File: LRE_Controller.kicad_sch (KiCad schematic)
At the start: 14 parts, among them U1 TPS56A37RPAR

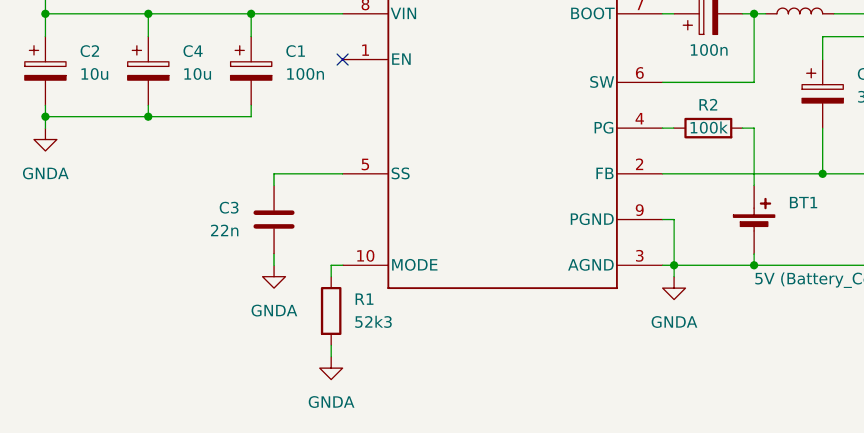
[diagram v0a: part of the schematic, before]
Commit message: Added Microcontroller and pressure transducer.
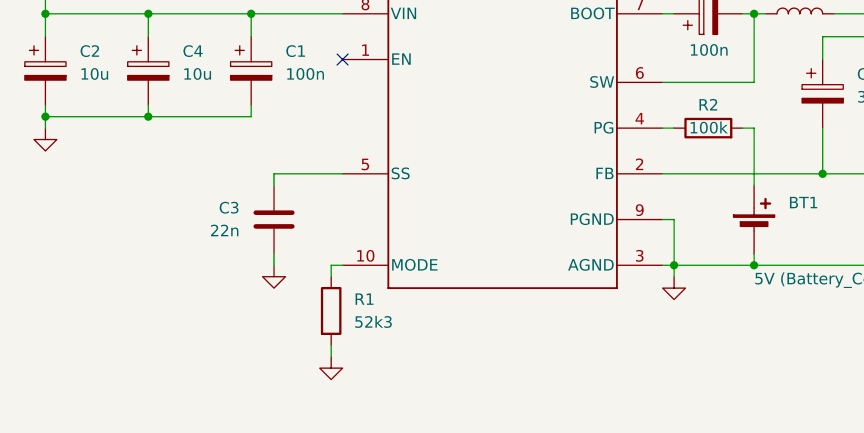
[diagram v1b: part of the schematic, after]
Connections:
- net GNDA renamed GND

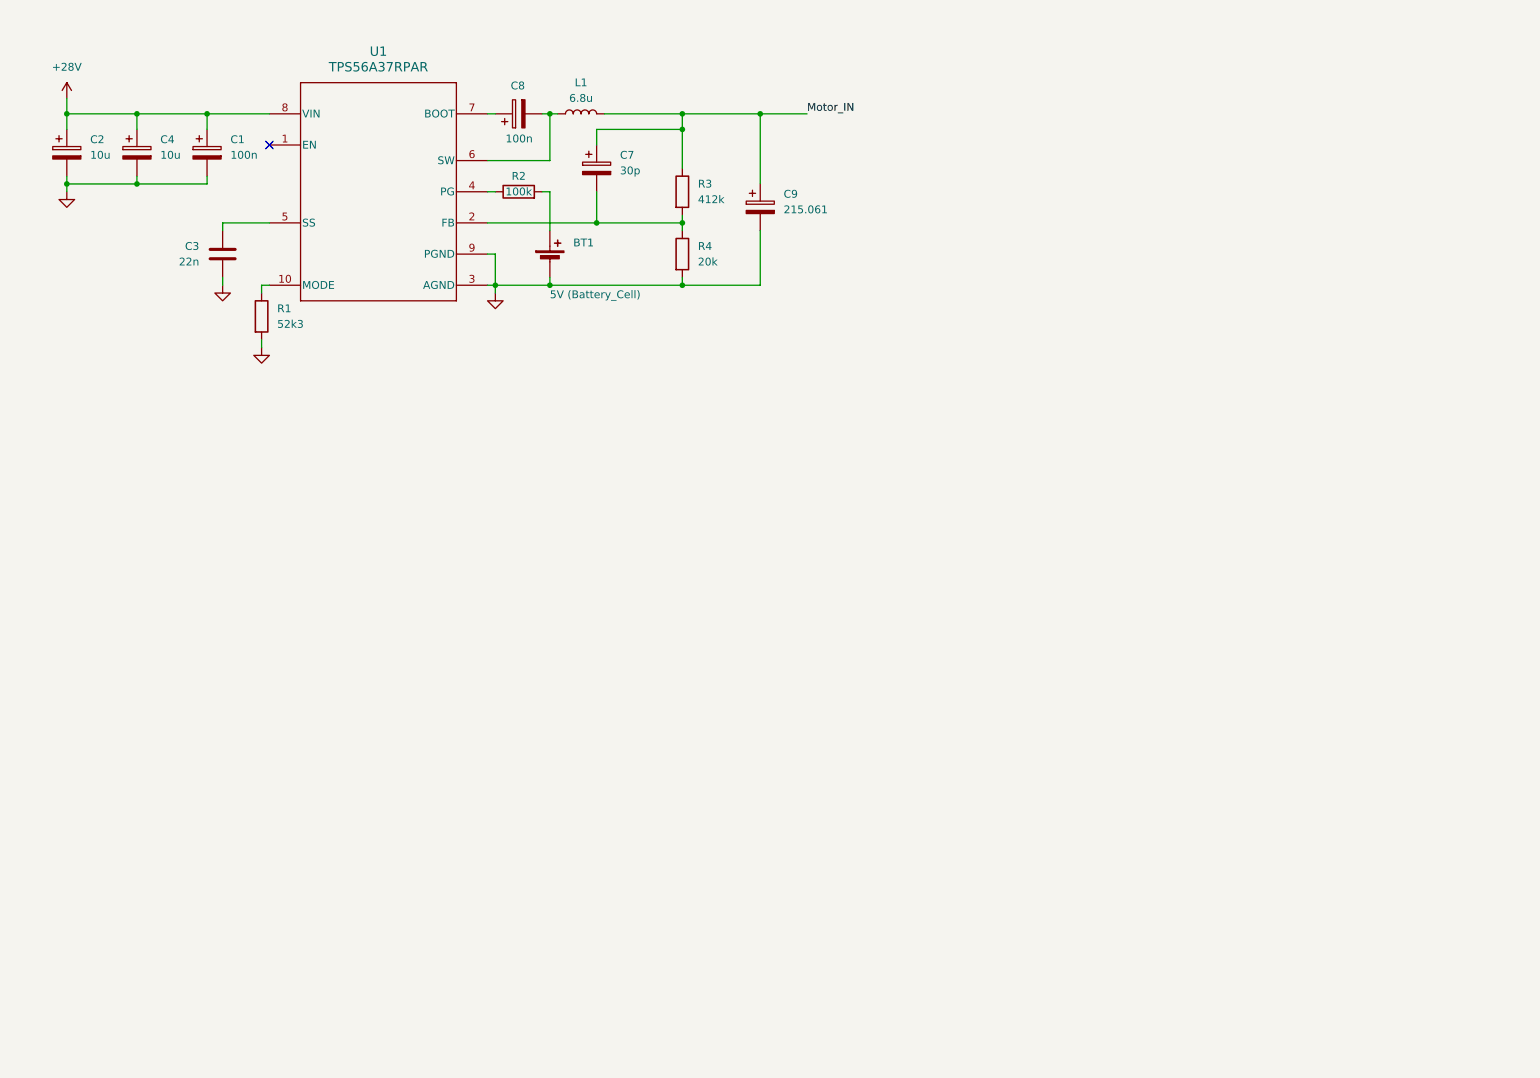
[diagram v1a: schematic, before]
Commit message: Restore schematics from local history
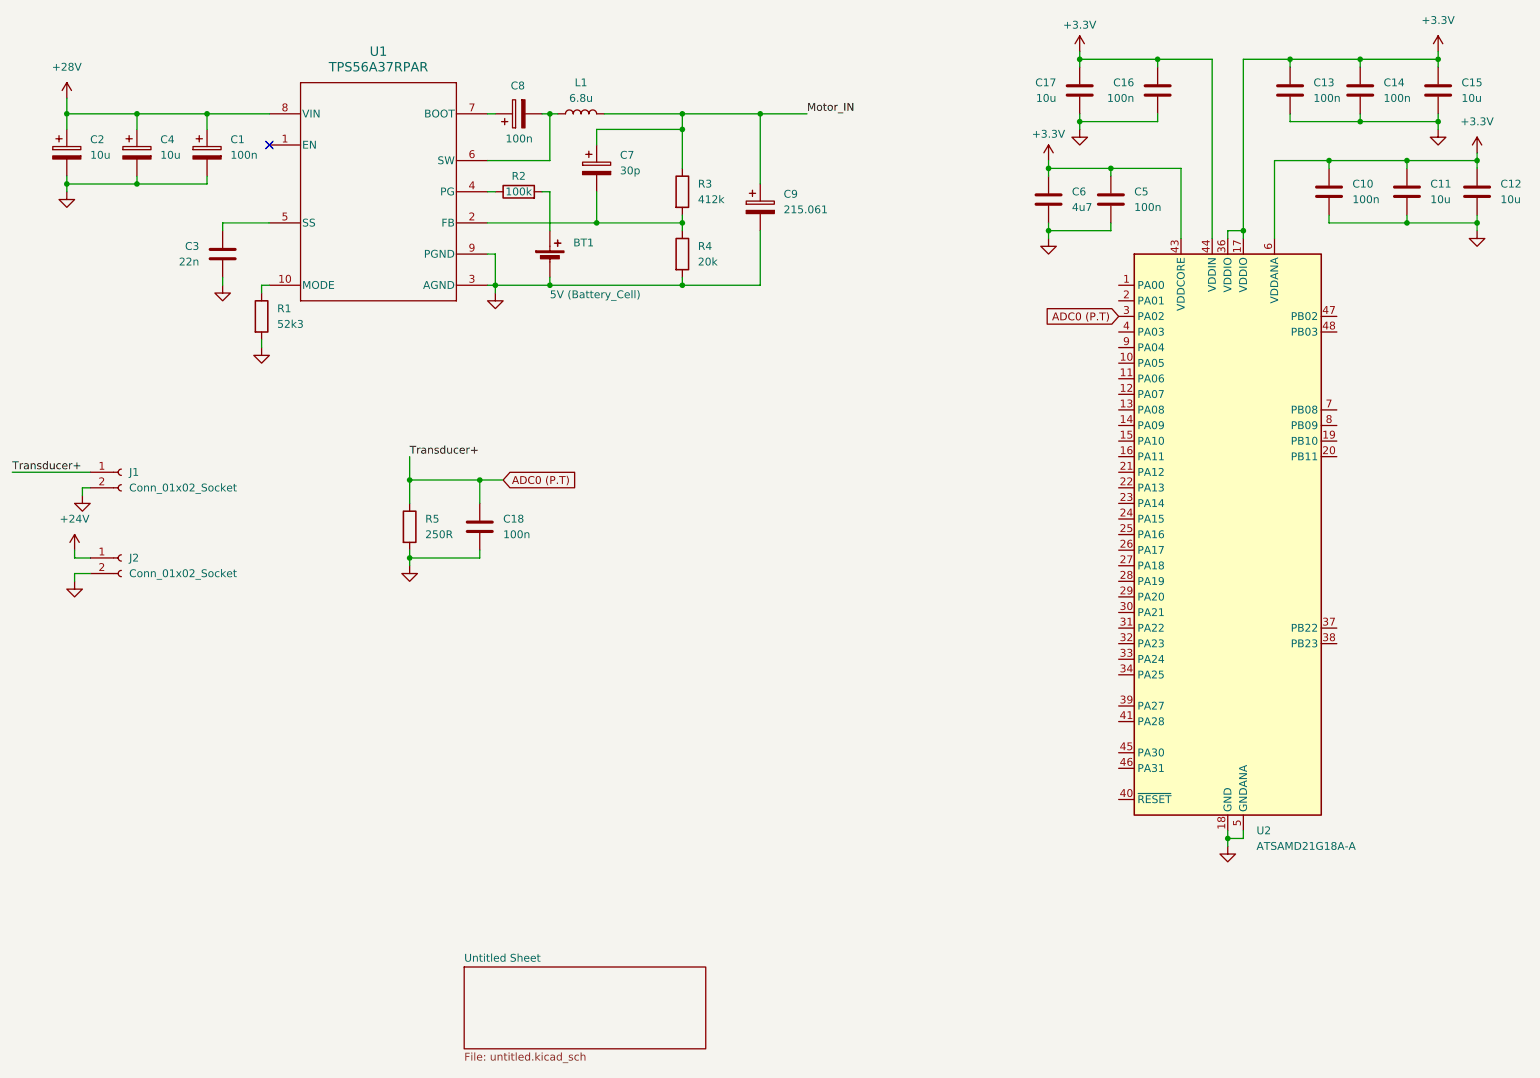
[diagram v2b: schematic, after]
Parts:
- added C10, C13, C14, C16, C18, C5: 100n, symbol Device:C
- added C11, C12, C15, C17: 10u, symbol Device:C
- added C6: 4u7, symbol Device:C
- added J1, J2: Conn_01x02_Socket, symbol Connector:Conn_01x02_Socket
- added R5: 250R, symbol Device:R
- added U2: ATSAMD21G18A-A, Package_QFP:TQFP-48_7x7mm_P0.5mm, symbol MCU_Microchip_SAMD:ATSAMD21G18A-A
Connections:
- net GND: now also C10.2, C11.2, C12.2, C13.2, C14.2, C15.2, C16.2, C17.2, C18.2, C5.2, C6.2, J1.2 (Pin_2), J2.2 (Pin_2), R5.2, U2.18 (GND), U2.35 (GND), U2.42 (GND), U2.5 (GNDANA)
- new net +24V: J2.1 (Pin_1)
- new net +3.3V: C10.1, C11.1, C12.1, C13.1, C14.1, C15.1, C16.1, C17.1, C5.1, C6.1, U2.17 (VDDIO), U2.36 (VDDIO), U2.43 (VDDCORE), U2.44 (VDDIN), U2.6 (VDDANA)
- new net ADC0 (P.T): C18.1, J1.1 (Pin_1), R5.1, U2.3 (PA02)
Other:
- added sheet Untitled Sheet (untitled.kicad_sch)

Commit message: Make block diagram the root sheet
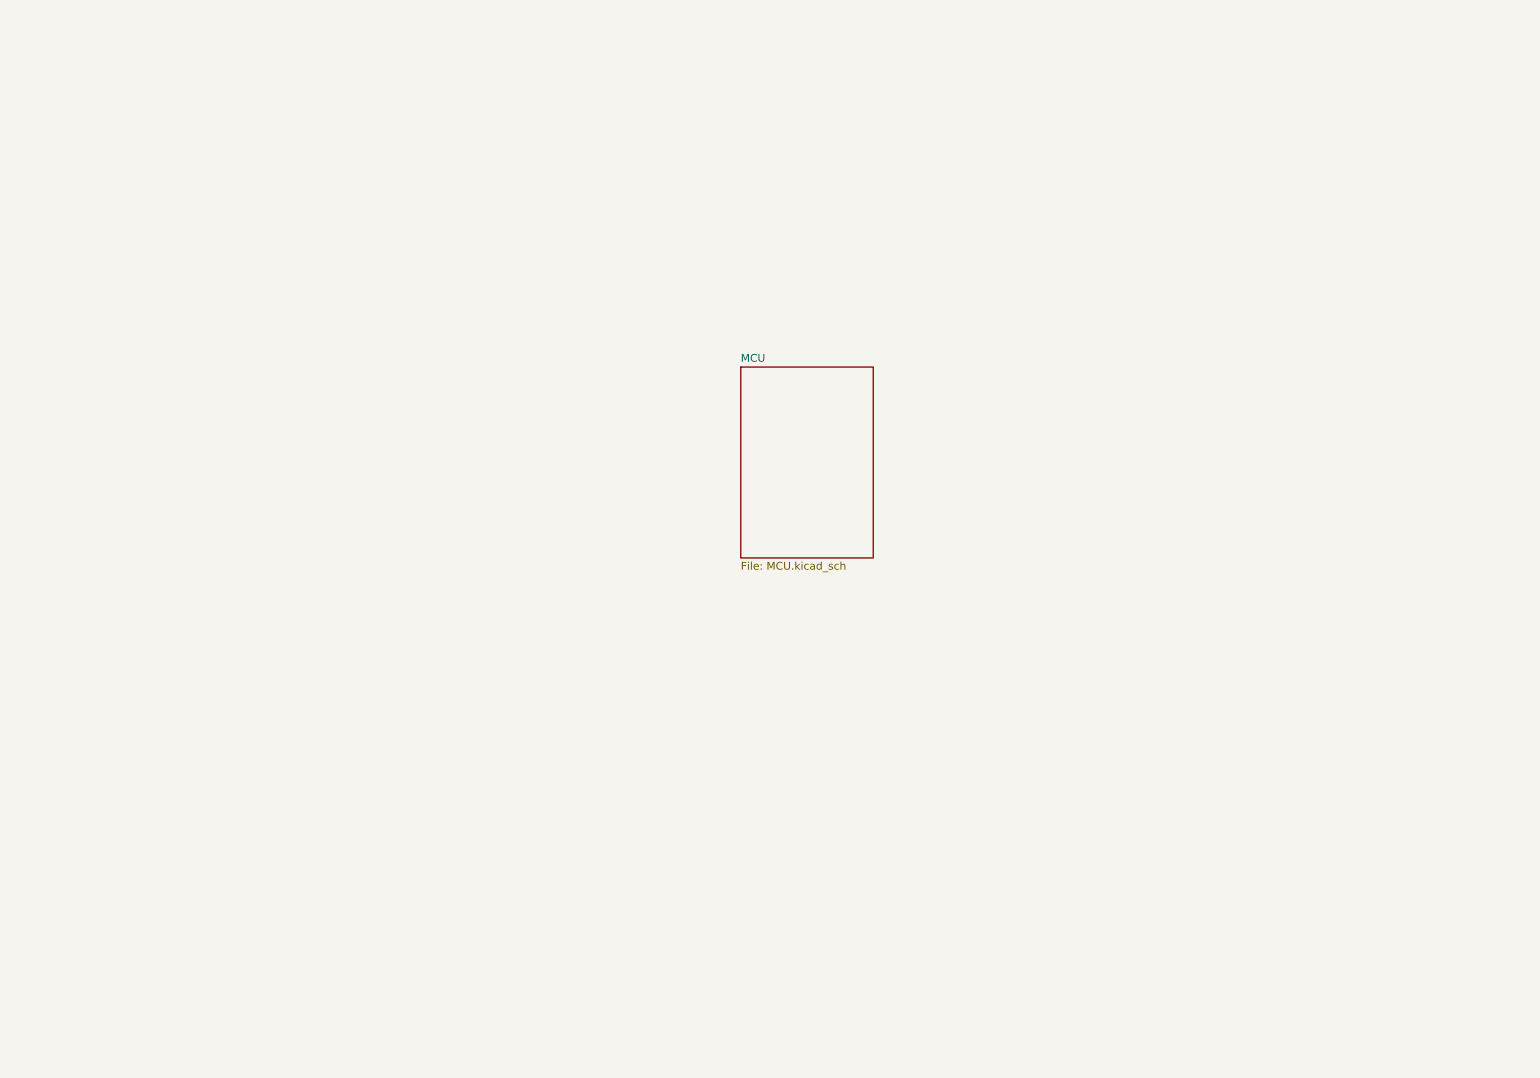
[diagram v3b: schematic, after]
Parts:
- removed BT1: 5V (Battery_Cell), symbol Device:Battery_Cell
- removed C1, C8: 100n, symbol Device:C_Polarized
- removed C10, C13, C14, C16, C18, C5: 100n, symbol Device:C
- removed C11, C12, C15, C17: 10u, symbol Device:C
- removed C2, C4: 10u, symbol Device:C_Polarized
- removed C3: 22n, symbol Device:C
- removed C6: 4u7, symbol Device:C
- removed C7: 30p, symbol Device:C_Polarized
- removed C9: 215.061, symbol Device:C_Polarized
- removed J1, J2: Conn_01x02_Socket, symbol Connector:Conn_01x02_Socket
- removed L1: 6.8u, symbol Device:L
- removed R1: 52k3, symbol Device:R
- removed R2: 100k, symbol Device:R
- removed R3: 412k, symbol Device:R
- removed R4: 20k, symbol Device:R
- removed R5: 250R, symbol Device:R
- removed U1: TPS56A37RPAR, RPA0010A-MFG, symbol Imported_ICs:TPS56A37RPAR
- removed U2: ATSAMD21G18A-A, Package_QFP:TQFP-48_7x7mm_P0.5mm, symbol MCU_Microchip_SAMD:ATSAMD21G18A-A
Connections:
- no-connect marks 1 -> 0
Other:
- removed sheet Untitled Sheet
- added sheet MCU (MCU.kicad_sch)

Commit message: Added USB C, LDO regulator and sections off schematic in pages to make readable
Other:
- added sheet Connectors (Connectors.kicad_sch)
- added sheet Sensors (Sensors.kicad_sch)
- added sheet buck_converter/LDO (TPS56A37RPAR.kicad_sch)

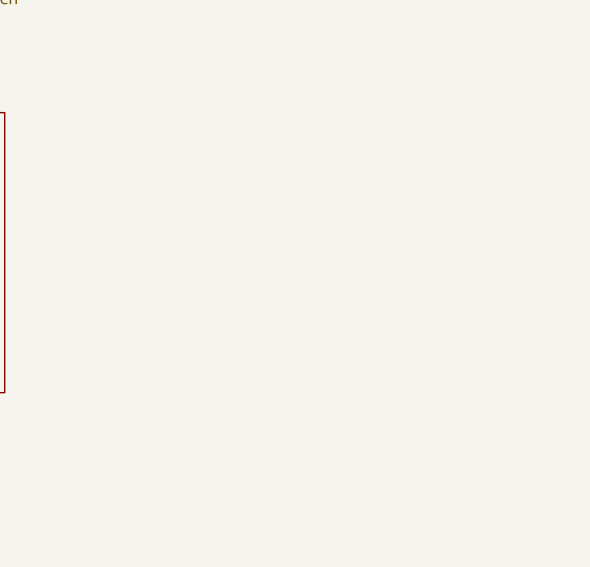
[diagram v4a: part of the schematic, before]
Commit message: Added solenoid valve circuit
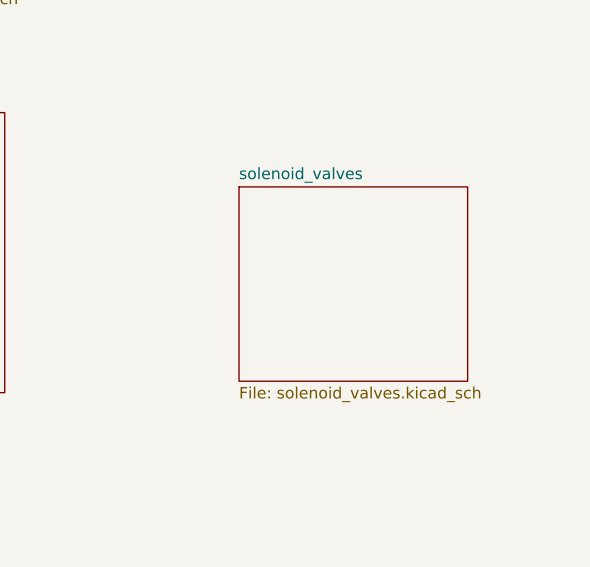
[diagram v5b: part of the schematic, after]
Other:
- added sheet solenoid_valves (solenoid_valves.kicad_sch)
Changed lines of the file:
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@@
+	)
+	(sheet
+		(at 184.15 87.63)
+		(size 25.4 21.59)
+		(exclude_from_sim no)
+		(in_bom yes)
+		(on_board yes)
+		(dnp no)
+		(fields_autoplaced yes)
+		(stroke
+			(width 0.1524)
+			(type solid)
+		)
+		(fill
+			(color 0 0 0 0)
+		)
+		(property "Sheetname" "solenoid_valves"
+			(at 184.15 86.9184 0)
+			(show_name no)
+			(do_not_autoplace no)
+			(effects
+				(font
+					(size 1.27 1.27)
+				)
+				(justify left bottom)
+			)
+		)
+		(property "Sheetfile" "solenoid_valves.kicad_sch"
+			(at 184.15 109.8046 0)
+			(show_name no)
+			(do_not_autoplace no)
+			(effects
+				(font
+					(size 1.27 1.27)
+				)
+				(justify left top)
+			)
+		)
+		(instances
+			(project "LRE_Controller"
+				(path "/b27bef7b-72d9-475e-9417-80b6d20be6a1"
+					(page "6")
+				)
+			)
+		)
 	)
 	(sheet
@@
 			)
 		)
+		(instances
+			(project "LRE_Controller"
+				(path "/b27bef7b-72d9-475e-9417-80b6d20be6a1"
+					(page "5")
+				)
+			)
+		)
